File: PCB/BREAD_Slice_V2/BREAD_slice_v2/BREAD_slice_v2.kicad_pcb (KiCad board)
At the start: 2 copper layers, 70.6 x 100 mm, 36 parts, among them J1 10018783-10200TLF, J10 Screw_Terminal_01x04, J11 Screw_Terminal_01x04, J2 Screw_Terminal_01x04, J3 Conn_01x03_Male, J4 Conn_01x06_Socket, J5 Screw_Terminal_01x02, J6 Conn_01x02_Socket, J7 Conn_01x10_Socket, J8 Screw_Terminal_01x04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

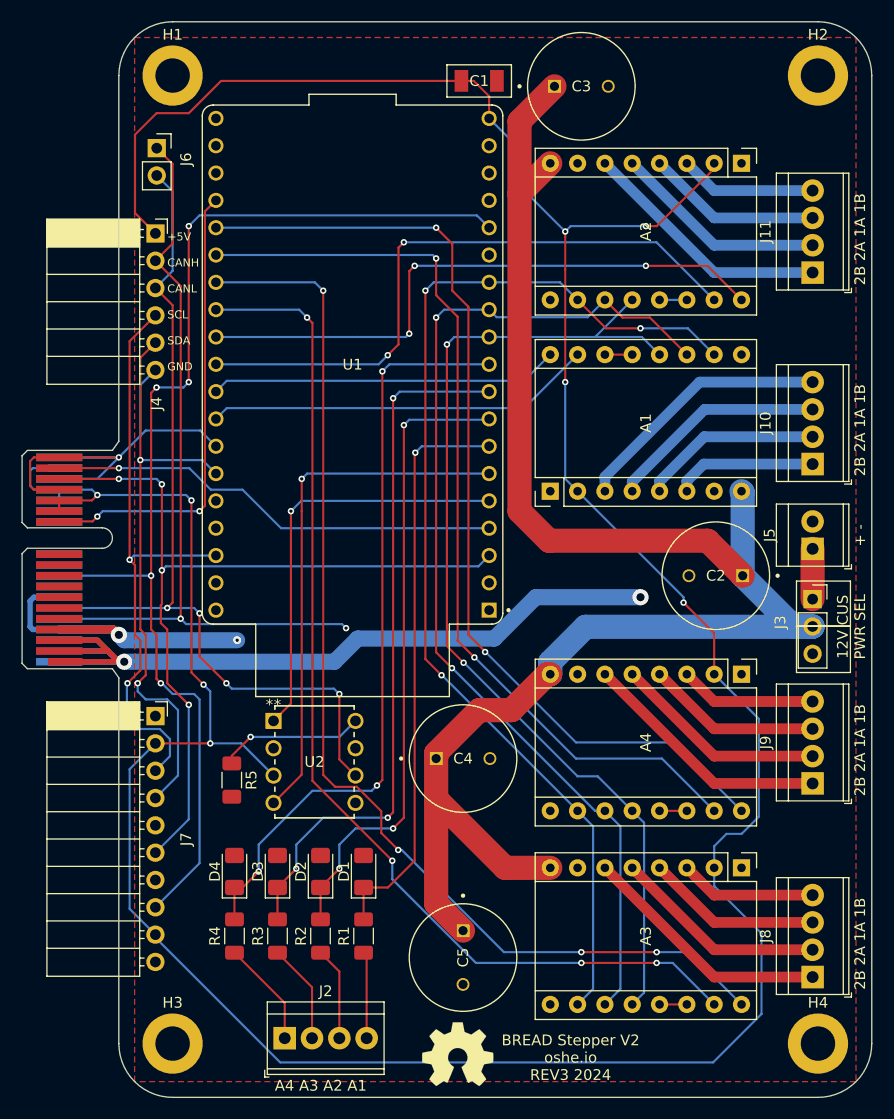
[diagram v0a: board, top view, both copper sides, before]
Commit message: fixed can tx/rx on input only pins
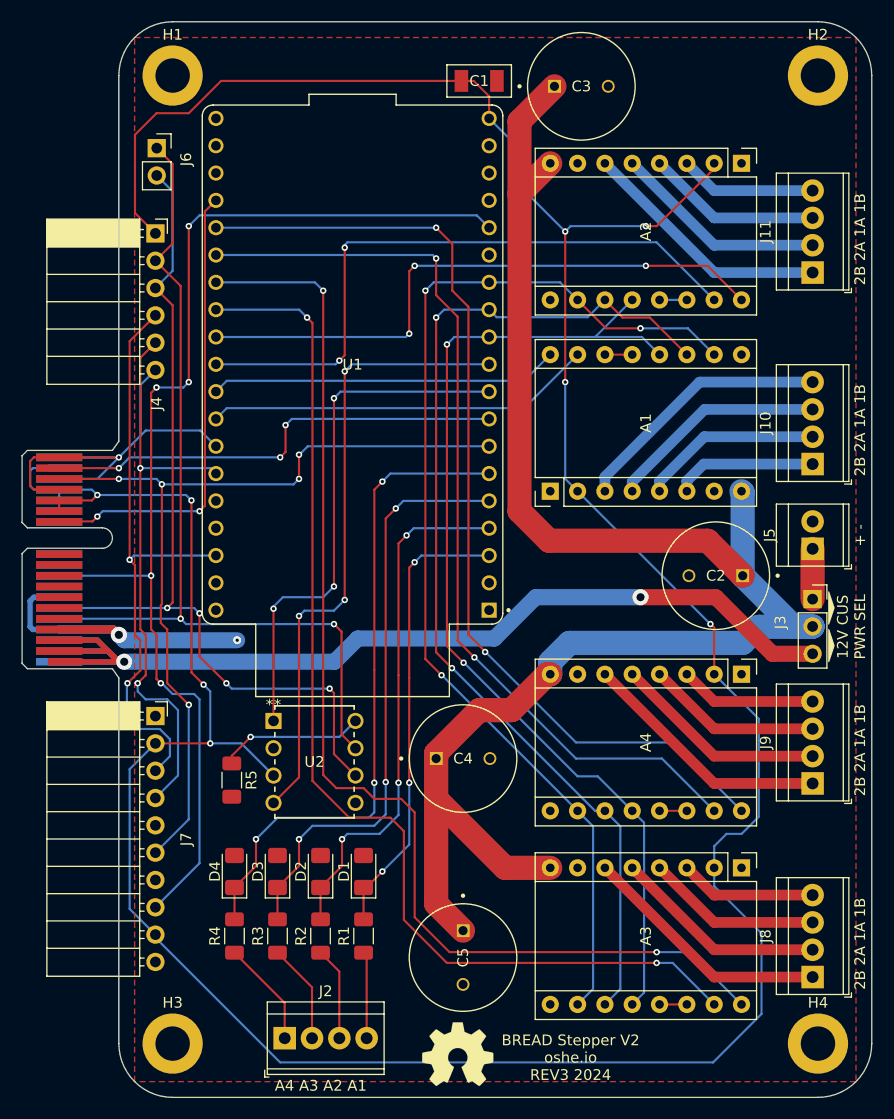
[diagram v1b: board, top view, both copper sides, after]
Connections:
- U1 pad J2_10: /AG_4 -> /RX
- U1 pad J2_3: /EstpCh1 -> /AG_1
- U1 pad J2_4: /EstpCh2 -> /AG_2
- U1 pad J2_5: /TX -> /AG_3
- U1 pad J2_6: /RX -> /AG_4
- U1 pad J2_7: /AG_1 -> /EstpCh1
- U1 pad J2_8: /AG_2 -> /EstpCh2
- U1 pad J2_9: /AG_3 -> /TX
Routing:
- net +12V: track 87.7 -> 105.9 mm
- net /AG_1: track 54.1 -> 42.5 mm, vias 1 -> 3
- net /CANH: track 73.0 -> 84.1 mm
- net /AG_2: track 59.4 -> 48.7 mm
- net /AG_3: track 65.6 -> 55.2 mm
- net /TX: track 39.1 -> 49.2 mm, vias 1 -> 3
- net /RX: track 49.0 -> 58.3 mm, vias 1 -> 3
- net /AG_4: track 70.5 -> 61.6 mm
- net /DR_3: track 104.2 -> 108.8 mm, vias 4 -> 2
- net /ST_3: track 99.0 -> 102.9 mm, vias 4 -> 2
- net /EstpCh1: track 77.4 -> 79.6 mm, vias 4 -> 5
- net /EstpCh2: track 42.3 -> 43.3 mm, vias 1 -> 3
- net /ST_2: track 58.5 -> 59.2 mm
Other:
- board text removed: "+5V CANH CANL SCL SDA GND"
